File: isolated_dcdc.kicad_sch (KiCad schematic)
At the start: 15 parts, among them U6 LMR51610, U7 NXE2S0505MC, U8 NCP1117-3.3_SOT223

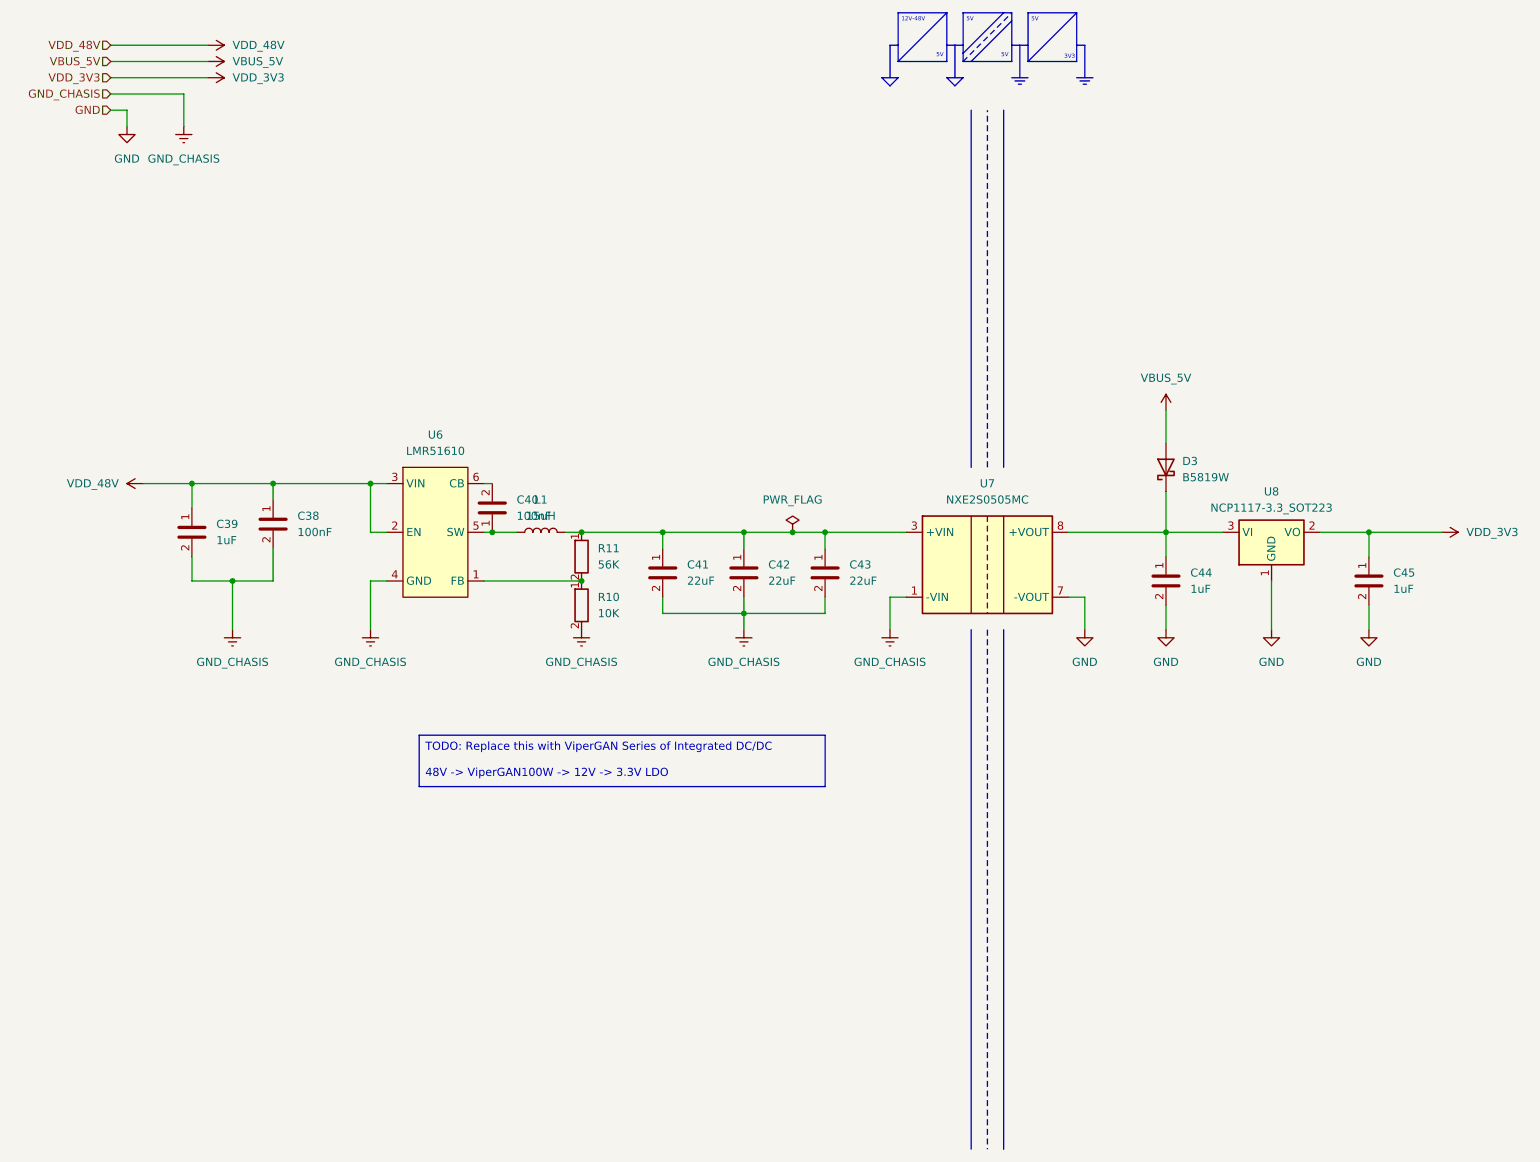
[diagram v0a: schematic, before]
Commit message: fix(eth_phy): completed revamp with lan8742a
BREAKING CHANGE:
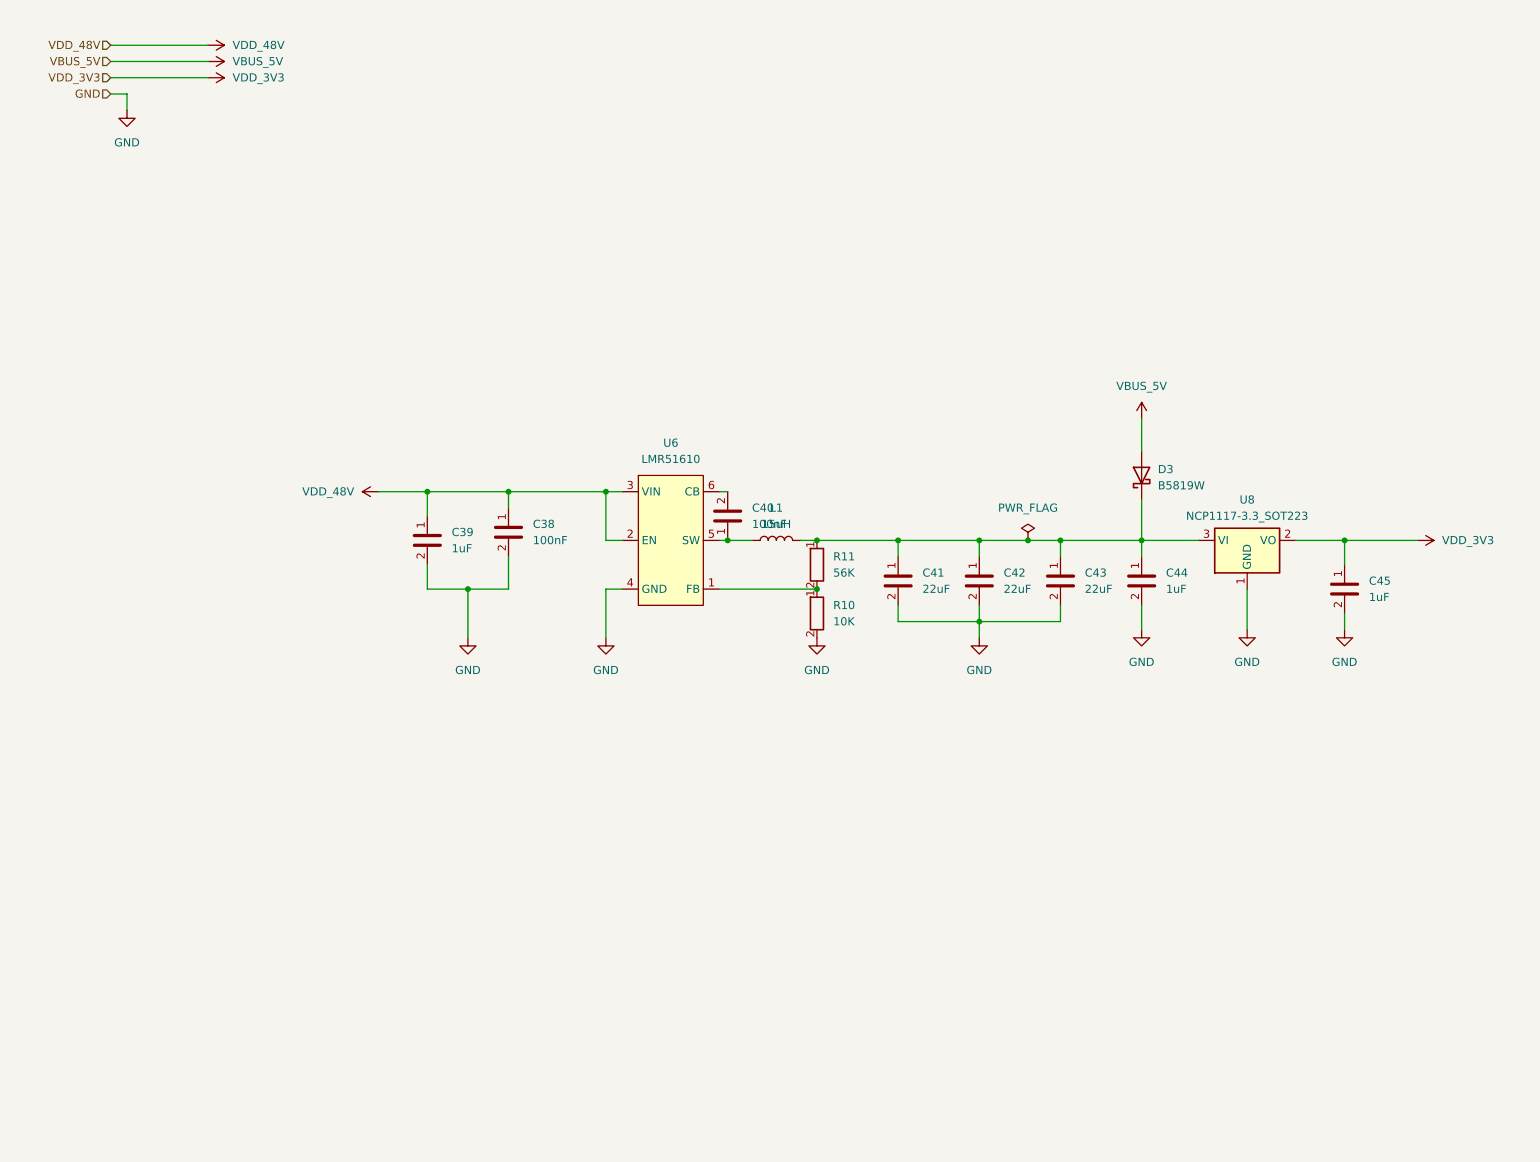
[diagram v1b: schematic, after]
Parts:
- removed U7: NXE2S0505MC, Converter_DCDC:Converter_DCDC_Murata_NXExSxxxxMC_SMD, symbol 0_chenry_lib:NXE2S0505MC
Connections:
- net GND_CHASIS is gone; now on net GND: C38.2, C39.2, C41.2, C42.2, C43.2, R10.2, U6.4 (GND)
- net at C44.1, D3.1 (K), U8.3 (VI): now also C41.1, C42.1, C43.1, L1.2, R11.1
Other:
- note removed: "12V-48V"
- note removed: "3V3"
- note removed: "5V"
- moved on the sheet: C38, C39, C40, C41, C42, C43, C44, C45, D3, L1, R10, R11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
